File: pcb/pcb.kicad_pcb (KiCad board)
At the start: 2 copper layers, 75 x 75 mm, 4 parts, among them U1 1117-3.3

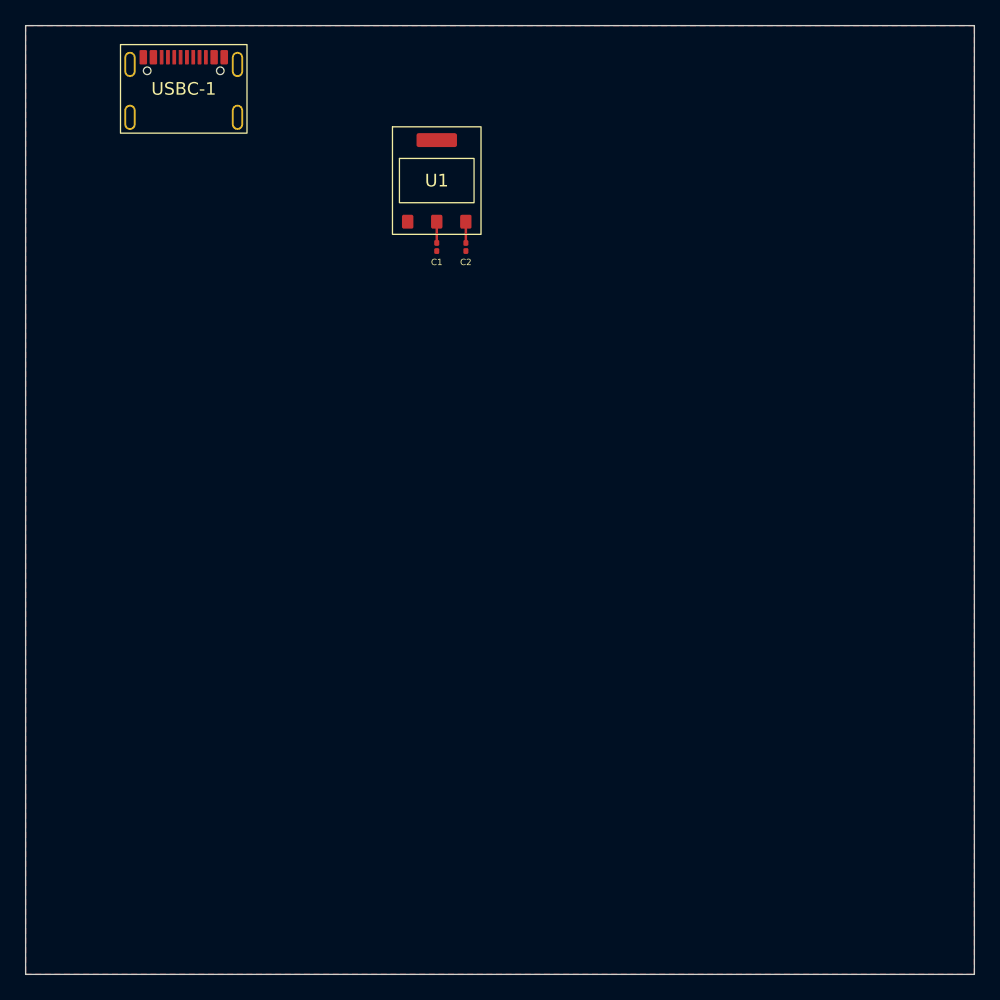
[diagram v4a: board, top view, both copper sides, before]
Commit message: add vias and ground
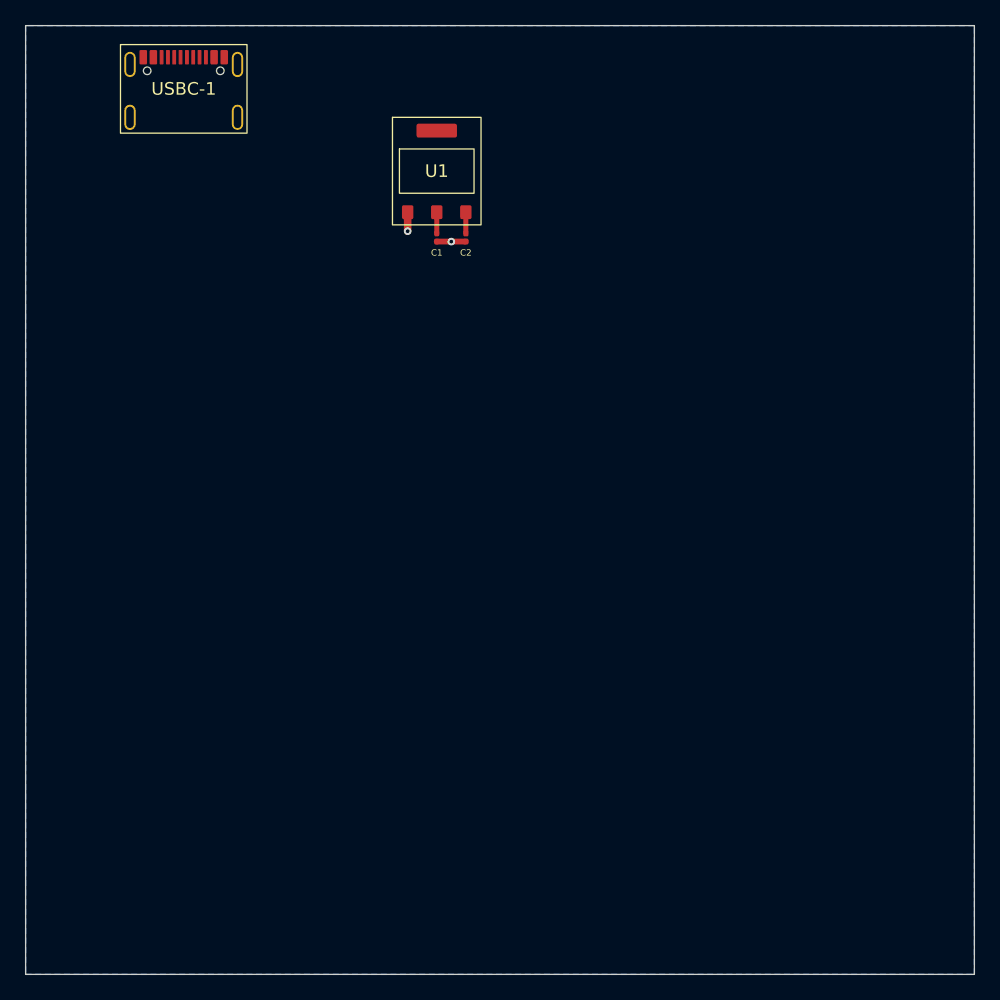
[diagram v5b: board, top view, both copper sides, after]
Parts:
- moved C1 0.75 mm to (32.5, 16.8)
- moved C2 0.75 mm to (34.8, 16.8)
- moved U1 0.75 mm to (32.5, 14.8)
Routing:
- net GND: track 0.00 -> 3.80 mm, vias 0 -> 2
- added copper zone on B.Cu, net GND
- removed copper zone on F.Cu, net GND
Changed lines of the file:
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@@
 	(footprint "Capacitor_SMD:C_0201_0603Metric"
 		(layer "F.Cu")
-		(at 32.5 17.5 90)
+		(at 32.5 16.75 90)
 		(descr "Capacitor SMD 0201 (0603 Metric), square (rectangular) end terminal, IPC-7351 nominal, (Body size source: https://www.vishay.com/docs/20052/crcw0201e3.pdf)")
 		(tags "capacitor")
@@
 	(footprint "Andrews_Library:LCSC_SMD_1117-3.3v_C5125088"
 		(layer "F.Cu")
-		(at 32.5 15.5)
+		(at 32.5 14.75)
 		(property "Reference" "U1"
 			(at 0 -3.25 0)
@@
 			(polygon
 				(pts
-					(xy 29 8) (xy 36 8) (xy 36 16.5) (xy 29 16.5)
+					(xy 29 7.25) (xy 36 7.25) (xy 36 15.75) (xy 29 15.75)
 				)
 			)
@@
 	(footprint "Capacitor_SMD:C_0201_0603Metric"
 		(layer "F.Cu")
-		(at 34.8 17.5 -90)
+		(at 34.8 16.75 -90)
 		(descr "Capacitor SMD 0201 (0603 Metric), square (rectangular) end terminal, IPC-7351 nominal, (Body size source: https://www.vishay.com/docs/20052/crcw0201e3.pdf)")
 		(tags "capacitor")
@@
 	)
 	(segment
-		(start 32.5 15.5)
-		(end 32.5 17.18)
+		(start 33.655 17.07)
+		(end 33.65 17.075)
 		(width 0.2)
 		(layer "F.Cu")
+		(net "GND")
+	)
+	(segment
+		(start 33.645 17.07)
+		(end 33.65 17.075)
+		(width 0.2)
+		(layer "F.Cu")
+		(net "GND")
+	)
+	(segment
+		(start 32.5 17.07)
+		(end 33.645 17.07)
+		(width 0.46)
+		(layer "F.Cu")
+		(net "GND")
+	)
+	(segment
+		(start 30.2 14.75)
+		(end 30.2 16.25)
+		(width 0.6)
+		(layer "F.Cu")
+		(net "GND")
+	)
+	(segment
+		(start 34.8 17.07)
+		(end 33.655 17.07)
+		(width 0.46)
+		(layer "F.Cu")
+		(net "GND")
+	)
+	(via
+		(at 30.2 16.25)
+		(size 0.6)
+		(drill 0.3)
+		(layers "F.Cu" "B.Cu")
+		(free yes)
+		(net "GND")
+	)
+	(via
+		(at 33.65 17.075)
+		(size 0.6)
+		(drill 0.3)
+		(layers "F.Cu" "B.Cu")
+		(free yes)
+		(net "GND")
+	)
+	(segment
+		(start 32.5 14.75)
+		(end 32.5 16.43)
+		(width 0.4)
+		(layer "F.Cu")
 		(net "VBUS")
 	)
 	(segment
-		(start 34.8 15.5)
-		(end 34.8 17.18)
-		(width 0.2)
+		(start 34.8 14.75)
+		(end 34.8 16.43)
+		(width 0.4)
 		(layer "F.Cu")
 		(net "Net-(U1-VIN)")
@@
 	(zone
 		(net "GND")
-		(layer "F.Cu")
+		(layer "B.Cu")
 		(hatch edge 0.5)
 		(connect_pads
@@
 		)
 	)
-	(group ""
-		(members "4c363494-5d20-44a3-9b12-37bc64127a15" "7ff470fd-2abd-486a-b746-3b467e71a7f8"
-			"a43b688b-cef3-4c08-969a-ef6623efc0b7" "c16a55e6-c9ba-4bf5-9418-845e8fc3c2c0"
-			"e2951551-5bd3-452b-943a-e5c31ddf3bfe"
-		)
-	)

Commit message: usbc schematic done?
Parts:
- moved C1 18.0 mm to (15.5, 10.7)
- moved U1 18.0 mm to (15.5, 8.72)
- moved C2 18.0 mm to (17.8, 10.7)
- moved USBC-1 6.52 mm to (6.00, 4.50)
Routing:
- net VBUS: track 1.68 -> 8.13 mm
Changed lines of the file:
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@@
 	(footprint "Capacitor_SMD:C_0201_0603Metric"
 		(layer "F.Cu")
-		(at 32.5 16.75 90)
+		(at 15.5 10.725 90)
 		(descr "Capacitor SMD 0201 (0603 Metric), square (rectangular) end terminal, IPC-7351 nominal, (Body size source: https://www.vishay.com/docs/20052/crcw0201e3.pdf)")
 		(tags "capacitor")
@@
 	(footprint "Andrews_Library:LCSC_SMD_USBC_C2760486"
 		(layer "F.Cu")
-		(at 12.5 5)
+		(at 6 4.5)
 		(property "Reference" "USBC-1"
 			(at 0 0 0)
@@
 		)
 		(property "Value" "TYPE-C-31-M-31"
-			(at 0 6.7 0)
-			(unlocked yes)
-			(layer "F.Fab")
+			(at 0 0 0)
+			(unlocked yes)
+			(layer "F.Fab")
+			(hide yes)
 			(effects
 				(font
@@
 		)
 		(fp_text user "${REFERENCE}"
-			(at 0 4.8 0)
+			(at 0 0 0)
 			(unlocked yes)
 			(layer "F.Fab")
@@
 	(footprint "Andrews_Library:LCSC_SMD_1117-3.3v_C5125088"
 		(layer "F.Cu")
-		(at 32.5 14.75)
+		(at 15.5 8.725)
 		(property "Reference" "U1"
 			(at 0 -3.25 0)
@@
 		)
 		(property "Value" "1117-3.3"
-			(at 0 -8.7 0)
-			(unlocked yes)
-			(layer "F.Fab")
+			(at 0 -3.25 0)
+			(unlocked yes)
+			(layer "F.Fab")
+			(hide yes)
 			(effects
 				(font
@@
 		)
 		(fp_text user "${REFERENCE}"
-			(at 0 -10.5 0)
+			(at 0 -3.25 0)
 			(unlocked yes)
 			(layer "F.Fab")
@@
 			(polygon
 				(pts
-					(xy 29 7.25) (xy 36 7.25) (xy 36 15.75) (xy 29 15.75)
+					(xy 12 1.225) (xy 19 1.225) (xy 19 9.725) (xy 12 9.725)
 				)
 			)
@@
 	(footprint "Capacitor_SMD:C_0201_0603Metric"
 		(layer "F.Cu")
-		(at 34.8 16.75 -90)
+		(at 17.8 10.725 -90)
 		(descr "Capacitor SMD 0201 (0603 Metric), square (rectangular) end terminal, IPC-7351 nominal, (Body size source: https://www.vishay.com/docs/20052/crcw0201e3.pdf)")
 		(tags "capacitor")
@@
 	)
 	(segment
-		(start 33.655 17.07)
-		(end 33.65 17.075)
+		(start 16.655 11.045)
+		(end 16.65 11.05)
 		(width 0.2)
 		(layer "F.Cu")
@@
 	)
 	(segment
-		(start 33.645 17.07)
-		(end 33.65 17.075)
+		(start 16.645 11.045)
+		(end 16.65 11.05)
 		(width 0.2)
 		(layer "F.Cu")
@@
 	)
 	(segment
-		(start 32.5 17.07)
-		(end 33.645 17.07)
+		(start 15.5 11.045)
+		(end 16.645 11.045)
 		(width 0.46)
 		(layer "F.Cu")
@@
 	)
 	(segment
-		(start 30.2 14.75)
-		(end 30.2 16.25)
+		(start 13.2 8.725)
+		(end 13.2 10.225)
 		(width 0.6)
 		(layer "F.Cu")
@@
 	)
 	(segment
-		(start 34.8 17.07)
-		(end 33.655 17.07)
+		(start 17.8 11.045)
+		(end 16.655 11.045)
 		(width 0.46)
 		(layer "F.Cu")
@@
 	)
 	(via
-		(at 30.2 16.25)
+		(at 13.2 10.225)
 		(size 0.6)
 		(drill 0.3)
@@
 	)
 	(via
-		(at 33.65 17.075)
+		(at 16.65 11.05)
 		(size 0.6)
 		(drill 0.3)
@@
 	)
 	(segment
-		(start 32.5 14.75)
-		(end 32.5 16.43)
+		(start 15.5 8.725)
+		(end 15.5 10.405)
 		(width 0.4)
 		(layer "F.Cu")
@@
 	)
 	(segment
-		(start 34.8 14.75)
-		(end 34.8 16.43)
+		(start 15.5 2.275)
+		(end 15.5 8.725)
+		(width 0.9)
+		(layer "F.Cu")
+		(net "VBUS")
+	)
+	(segment
+		(start 17.8 8.725)
+		(end 17.8 10.405)
 		(width 0.4)
 		(layer "F.Cu")
@@
 		)
 	)
+	(group ""
+		(members "39f46827-d604-4451-9185-d2c690da2b4b" "41b5fd87-8459-422c-bbc8-8b2f33a92733"
+			"4c363494-5d20-44a3-9b12-37bc64127a15" "60749c63-a4b9-4ef0-87bf-f6affbc0b8c7"
+			"7ff470fd-2abd-486a-b746-3b467e71a7f8" "a43b688b-cef3-4c08-969a-ef6623efc0b7"
+			"c16a55e6-c9ba-4bf5-9418-845e8fc3c2c0" "cd536c35-41a0-4b0b-8b86-075b95b23e07"
+			"cdebdc92-b3ab-437b-86b3-235f62b4ac51" "d3b7c60e-c1e7-4286-9bf0-45802d237ef3"
+			"d652f132-8de8-4c92-b180-d0c4723e5263" "dfa21c28-cfff-4090-87bf-47aef60440bb"
+			"e2951551-5bd3-452b-943a-e5c31ddf3bfe"
+		)
+	)

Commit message: usb c stuff
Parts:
- added R1: 27, Resistor_SMD:R_0201_0603Metric, F.Cu at (11.8, 9.50)
- added R2: 27, Resistor_SMD:R_0201_0603Metric, F.Cu at (12.8, 9.50)
- added R3: 5.1k, Resistor_SMD:R_0201_0603Metric, F.Cu at (13.8, 9.50)
- added R4: 5.1k, Resistor_SMD:R_0201_0603Metric, F.Cu at (10.8, 9.50)
- moved C1 22.4 mm to (32.7, 25.0)
- moved U1 22.4 mm to (32.7, 23.0)
- moved C2 22.4 mm to (35.0, 25.0)
- moved USBC-1 6.52 mm to (12.5, 5.00), turned to 180 degrees
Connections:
- USBC-1 pad A5: unconnected-(USBC-1-CC1-PadA5) -> Net-(USBC-1-CC1)
- USBC-1 pad A6: unconnected-(USBC-1-DP1-PadA6) -> Net-(USBC-1-DP1)
- USBC-1 pad A7: unconnected-(USBC-1-DN1-PadA7) -> Net-(USBC-1-DN1)
- USBC-1 pad B5: unconnected-(USBC-1-CC2-PadB5) -> Net-(USBC-1-CC2)
- USBC-1 pad B6: unconnected-(USBC-1-DP2-PadB6) -> Net-(USBC-1-DP1)
- USBC-1 pad B7: unconnected-(USBC-1-DN2-PadB7) -> Net-(USBC-1-DN1)
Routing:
- net (no net): track 0.00 -> 6.80 mm
- net Net-(USBC-1-DP1): track 0.00 -> 4.35 mm
- net Net-(USBC-1-DN1): track 0.00 -> 3.77 mm
- net GND: track 3.80 -> 5.66 mm, vias 2 -> 4
- net Net-(USBC-1-CC2): track 0.00 -> 1.68 mm
- net Net-(USBC-1-CC1): track 0.00 -> 1.68 mm

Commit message: fixxed usbc stuff
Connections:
- USBC-1 pad A1/B12: (no net) -> GND
- USBC-1 pad A4/B9: (no net) -> VBUS
- USBC-1 pad B1/A12: (no net) -> GND
- USBC-1 pad B4/A9: (no net) -> VBUS
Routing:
- net (no net): track 6.80 -> 0.00 mm
- net VBUS: track 8.13 -> 14.8 mm
- net GND: track 5.66 -> 8.24 mm
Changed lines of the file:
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@@
 			(at -1.2 0 180)
 			(layer "F.SilkS")
+			(hide yes)
 			(effects
 				(font
@@
 			(unit
 				(name "A")
-				(pins "A4" "A9" "1" "A8" "A1" "B8" "A12" "A6" "B6" "A7" "B7" "A5" "B5")
+				(pins "A4/B9" "B4/A9" "A8" "1" "B8" "A1/B12" "B1/A12" "A6" "B6" "A7"
+					"B7" "A5" "B5"
+				)
 			)
 		)
@@
 			(layers "F.Cu" "F.Mask" "F.Paste")
 			(roundrect_rratio 0.15)
+			(net "GND")
+			(pinfunction "GND_A1/B12")
+			(pintype "power_out")
 		)
 		(pad "A4/B9" smd roundrect
@@
 			(layers "F.Cu" "F.Mask" "F.Paste")
 			(roundrect_rratio 0.15)
+			(net "VBUS")
+			(pinfunction "VBUS_A4/B9")
+			(pintype "power_in")
 		)
 		(pad "A5" smd roundrect
@@
 			(layers "F.Cu" "F.Mask" "F.Paste")
 			(roundrect_rratio 0.15)
+			(net "GND")
+			(pinfunction "GND_B1/A12")
+			(pintype "power_in")
 		)
 		(pad "B4/A9" smd roundrect
@@
 			(layers "F.Cu" "F.Mask" "F.Paste")
 			(roundrect_rratio 0.15)
+			(net "VBUS")
+			(pinfunction "VBUS_B4/A9")
+			(pintype "power_in")
 		)
 		(pad "B5" smd roundrect
@@
 			(pinfunction "SBU2_B8")
 			(pintype "bidirectional+no_connect")
+		)
+		(zone
+			(layer "F.SilkS")
+			(hatch edge 0.5)
+			(connect_pads
+				(clearance 0)
+			)
+			(min_thickness 0.25)
+			(keepout
+				(tracks allowed)
+				(vias allowed)
+				(pads allowed)
+				(copperpour allowed)
+				(footprints not_allowed)
+			)
+			(placement
+				(enabled no)
+				(sheetname "")
+			)
+			(fill
+				(thermal_gap 0.5)
+				(thermal_bridge_width 0.5)
+				(island_removal_mode 0)
+			)
+			(polygon
+				(pts
+					(xy 17.5 8.5) (xy 7.5 8.5) (xy 7.5 1.5) (xy 17.5 1.5)
+				)
+			)
 		)
 		(embedded_fonts no)
@@
 			(at 1.2 0 0)
 			(layer "F.SilkS")
+			(hide yes)
 			(effects
 				(font
@@
 	)
 	(segment
-		(start 10.1 7.5)
-		(end 10.1 6.889428)
-		(width 0.4)
-		(layer "F.Cu")
-		(net "")
-	)
-	(segment
-		(start 13.960572 5.95)
-		(end 14.9 6.889428)
-		(width 0.4)
-		(layer "F.Cu")
-		(net "")
-	)
-	(segment
-		(start 11.039428 5.95)
-		(end 13.960572 5.95)
-		(width 0.4)
-		(layer "F.Cu")
-		(net "")
-	)
-	(segment
-		(start 14.9 6.889428)
-		(end 14.9 7.5)
-		(width 0.4)
-		(layer "F.Cu")
-		(net "")
-	)
-	(segment
-		(start 10.1 6.889428)
-		(end 11.039428 5.95)
-		(width 0.4)
-		(layer "F.Cu")
-		(net "")
-	)
-	(segment
 		(start 13.75 9.82)
 		(end 13.75 10.75)
@@
 	)
 	(segment
+		(start 15.7 7.5)
+		(end 16.18 7.5)
+		(width 0.6)
+		(layer "F.Cu")
+		(net "GND")
+	)
+	(segment
 		(start 33.845 25.32)
 		(end 33.85 25.325)
 		(width 0.2)
+		(layer "F.Cu")
+		(net "GND")
+	)
+	(segment
+		(start 9.3 7.5)
+		(end 8.82 7.5)
+		(width 0.6)
+		(layer "F.Cu")
+		(net "GND")
+	)
+	(segment
+		(start 8.82 7.5)
+		(end 8.25 6.93)
+		(width 0.6)
+		(layer "F.Cu")
+		(net "GND")
+	)
+	(segment
+		(start 16.18 7.5)
+		(end 16.75 6.93)
+		(width 0.6)
 		(layer "F.Cu")
 		(net "GND")
@@
 	)
 	(segment
+		(start 13.75 9.18)
+		(end 13.75 7.5)
+		(width 0.3)
+		(layer "F.Cu")
+		(net "Net-(USBC-1-CC1)")
+	)
+	(segment
+		(start 14.019999 6.05)
+		(end 14.9 6.930001)
+		(width 0.4)
+		(layer "F.Cu")
+		(net "VBUS")
+	)
+	(segment
+		(start 14.9 6.930001)
+		(end 14.9 7.5)
+		(width 0.4)
+		(layer "F.Cu")
+		(net "VBUS")
+	)
+	(segment
 		(start 32.7 23)
 		(end 32.7 24.68)
@@
 	)
 	(segment
+		(start 10.1 6.930001)
+		(end 10.980001 6.05)
+		(width 0.4)
+		(layer "F.Cu")
+		(net "VBUS")
+	)
+	(segment
+		(start 10.980001 6.05)
+		(end 14.019999 6.05)
+		(width 0.4)
+		(layer "F.Cu")
+		(net "VBUS")
+	)
+	(segment
 		(start 32.7 16.55)
 		(end 32.7 23)
@@
 	)
 	(segment
+		(start 10.1 7.5)
+		(end 10.1 6.930001)
+		(width 0.4)
+		(layer "F.Cu")
+		(net "VBUS")
+	)
+	(segment
+		(start 12.75 7.5)
+		(end 12.75 6.75)
+		(width 0.3)
+		(layer "F.Cu")
+		(net "Net-(USBC-1-DP1)")
+	)
+	(segment
+		(start 12.5 6.5)
+		(end 12.06014 6.5)
+		(width 0.3)
+		(layer "F.Cu")
+		(net "Net-(USBC-1-DP1)")
+	)
+	(segment
+		(start 11.75 6.81014)
+		(end 11.75 7.5)
+		(width 0.3)
+		(layer "F.Cu")
+		(net "Net-(USBC-1-DP1)")
+	)
+	(segment
+		(start 12.06014 6.5)
+		(end 11.75 6.81014)
+		(width 0.3)
+		(layer "F.Cu")
+		(net "Net-(USBC-1-DP1)")
+	)
+	(segment
+		(start 11.75 7.5)
+		(end 11.75 9.18)
+		(width 0.3)
+		(layer "F.Cu")
+		(net "Net-(USBC-1-DP1)")
+	)
+	(segment
+		(start 12.75 6.75)
+		(end 12.5 6.5)
+		(width 0.3)
+		(layer "F.Cu")
+		(net "Net-(USBC-1-DP1)")
+	)
+	(segment
+		(start 13.25 8.68)
+		(end 13.25 7.5)
+		(width 0.3)
+		(layer "F.Cu")
+		(net "Net-(USBC-1-DN1)")
+	)
+	(segment
+		(start 12.75 9.18)
+		(end 12.25 8.68)
+		(width 0.3)
+		(layer "F.Cu")
+		(net "Net-(USBC-1-DN1)")
+	)
+	(segment
+		(start 12.25 8.68)
+		(end 12.25 7.5)
+		(width 0.3)
+		(layer "F.Cu")
+		(net "Net-(USBC-1-DN1)")
+	)
+	(segment
+		(start 12.75 9.18)
+		(end 13.25 8.68)
+		(width 0.3)
+		(layer "F.Cu")
+		(net "Net-(USBC-1-DN1)")
+	)
+	(segment
 		(start 35 23)
 		(end 35 24.68)
@@
 		(layer "F.Cu")
 		(net "Net-(U1-VIN)")
-	)
-	(segment
-		(start 12.75 7.5)
-		(end 12.75 6.75)
-		(width 0.3)
-		(layer "F.Cu")
-		(net "Net-(USBC-1-DP1)")
-	)
-	(segment
-		(start 12.5 6.5)
-		(end 12.06014 6.5)
-		(width 0.3)
-		(layer "F.Cu")
-		(net "Net-(USBC-1-DP1)")
-	)
-	(segment
-		(start 11.75 6.81014)
-		(end 11.75 7.5)
-		(width 0.3)
-		(layer "F.Cu")
-		(net "Net-(USBC-1-DP1)")
-	)
-	(segment
-		(start 12.06014 6.5)
-		(end 11.75 6.81014)
-		(width 0.3)
-		(layer "F.Cu")
-		(net "Net-(USBC-1-DP1)")
-	)
-	(segment
-		(start 11.75 7.5)
-		(end 11.75 9.18)
-		(width 0.3)
-		(layer "F.Cu")
-		(net "Net-(USBC-1-DP1)")
-	)
-	(segment
-		(start 12.75 6.75)
-		(end 12.5 6.5)
-		(width 0.3)
-		(layer "F.Cu")
-		(net "Net-(USBC-1-DP1)")
-	)
-	(segment
-		(start 13.25 8.68)
-		(end 13.25 7.5)
-		(width 0.3)
-		(layer "F.Cu")
-		(net "Net-(USBC-1-DN1)")
-	)
-	(segment
-		(start 12.75 9.18)
-		(end 12.25 8.68)
-		(width 0.3)
-		(layer "F.Cu")
-		(net "Net-(USBC-1-DN1)")
-	)
-	(segment
-		(start 12.25 8.68)
-		(end 12.25 7.5)
-		(width 0.3)
-		(layer "F.Cu")
-		(net "Net-(USBC-1-DN1)")
-	)
-	(segment
-		(start 12.75 9.18)
-		(end 13.25 8.68)
-		(width 0.3)
-		(layer "F.Cu")
-		(net "Net-(USBC-1-DN1)")
-	)
-	(segment
-		(start 13.75 9.18)
-		(end 13.75 7.5)
-		(width 0.3)
-		(layer "F.Cu")
-		(net "Net-(USBC-1-CC1)")
 	)
 	(segment
@@
 	)
 	(group ""
-		(members "00969ec8-375b-461a-ab8d-53c311466271" "0a359fb5-a28c-437b-b3c2-884758fa63db"
-			"0c8b428b-1edc-46ec-a3d2-58d59bd35484" "0cf784ae-9619-49cc-926e-ad8379c289c3"
-			"1f80f27f-bd99-45b2-a851-89bcf631f704" "22f190ab-2413-41c7-a24e-e73d68eb9b5a"
-			"29bca4ab-ec63-4643-914a-e98f91e94fe1" "2a9f0b3c-4988-4b06-8d3b-91ca163887e9"
-			"2e3eb7c3-c9d2-411a-9390-10dacc6dc478" "3d43b053-7129-43c2-b6f8-94d0ffe57b91"
-			"42ab968e-dc35-4abf-b67d-e9f88bfc6e4c" "4b894bf6-9117-4017-9c98-93933f4364c6"
-			"50374173-e905-4b3e-b6d2-fd4c38eaf305" "6da9dd86-55fd-44dc-ad85-b6e9be5bf27e"
-			"7894b370-74d9-404b-9b6b-e3e80494a548" "80dcbed6-ae3c-4800-8257-a30dd492381d"
-			"8be4a25f-a4c5-4014-a745-92cac9a5666d" "9e8dbfe5-2635-42b1-bbe7-7b8837b5dda1"
-			"a210e89a-c73d-4a17-b1fd-acc9804ff3a6" "aeb65463-3c07-4a76-bf5e-a51c1b03362e"
-			"b25c3de0-fb7e-477a-af9d-b642d7986323" "c1df59e6-bd62-4538-8d3e-7d3726870be6"
-			"cf8427b6-465b-493e-9947-7a0465764b62" "d70bdebd-5174-401f-ab9f-6d77492b7c38"
-			"f601c40f-0a98-485b-a73e-e41fc2ebbc09" "faa3d2ee-5371-42f1-912d-1db73f624650"
+		(members "4c363494-5d20-44a3-9b12-37bc64127a15" "a4a7c4e0-1921-4a1c-82b8-160a991e9c46"
+			"c16a55e6-c9ba-4bf5-9418-845e8fc3c2c0"
 		)
 	)
 	(group ""
 		(members "39f46827-d604-4451-9185-d2c690da2b4b" "41b5fd87-8459-422c-bbc8-8b2f33a92733"
-			"4c363494-5d20-44a3-9b12-37bc64127a15" "60749c63-a4b9-4ef0-87bf-f6affbc0b8c7"
-			"7ff470fd-2abd-486a-b746-3b467e71a7f8" "a43b688b-cef3-4c08-969a-ef6623efc0b7"
-			"c16a55e6-c9ba-4bf5-9418-845e8fc3c2c0" "cd536c35-41a0-4b0b-8b86-075b95b23e07"
+			"60749c63-a4b9-4ef0-87bf-f6affbc0b8c7" "7ff470fd-2abd-486a-b746-3b467e71a7f8"
+			"a43b688b-cef3-4c08-969a-ef6623efc0b7" "cd536c35-41a0-4b0b-8b86-075b95b23e07"
 			"cdebdc92-b3ab-437b-86b3-235f62b4ac51" "d3b7c60e-c1e7-4286-9bf0-45802d237ef3"
 			"d652f132-8de8-4c92-b180-d0c4723e5263" "dfa21c28-cfff-4090-87bf-47aef60440bb"
@@
 		)
 	)
+	(group ""
+		(members "00969ec8-375b-461a-ab8d-53c311466271" "0a359fb5-a28c-437b-b3c2-884758fa63db"
+			"0c8b428b-1edc-46ec-a3d2-58d59bd35484" "0cf784ae-9619-49cc-926e-ad8379c289c3"
+			"22f190ab-2413-41c7-a24e-e73d68eb9b5a" "29bca4ab-ec63-4643-914a-e98f91e94fe1"
+			"29c53335-ca38-4edf-b1d0-7cbe707c089b" "2a9f0b3c-4988-4b06-8d3b-91ca163887e9"
+			"2e3eb7c3-c9d2-411a-9390-10dacc6dc478" "3d43b053-7129-43c2-b6f8-94d0ffe57b91"
+			"417895c3-bd0e-447a-942b-3d4d1012eba9" "42ab968e-dc35-4abf-b67d-e9f88bfc6e4c"
+			"4b894bf6-9117-4017-9c98-93933f4364c6" "5a9fd89b-1d9d-4b7a-a604-408fd6403691"
+			"6da9dd86-55fd-44dc-ad85-b6e9be5bf27e" "75d34a81-823b-4035-b028-19b2c1b16d58"
+			"7894b370-74d9-404b-9b6b-e3e80494a548" "7db35b0d-fab9-422b-8bb1-3db67172ce66"
+			"80dcbed6-ae3c-4800-8257-a30dd492381d" "88dfa8f3-c231-4c1e-8055-7ea4a8e82bd4"
+			"9e8dbfe5-2635-42b1-bbe7-7b8837b5dda1" "aeb65463-3c07-4a76-bf5e-a51c1b03362e"
+			"b25c3de0-fb7e-477a-af9d-b642d7986323" "c10a2b7c-0f63-4d39-bc5b-719cbd872340"
+			"cf8427b6-465b-493e-9947-7a0465764b62" "d1935751-456f-4883-a159-4dfe4b6ddd4c"
+			"d70bdebd-5174-401f-ab9f-6d77492b7c38" "deee6bf7-a490-4cca-a3b7-7114afd69a23"
+			"f601c40f-0a98-485b-a73e-e41fc2ebbc09" "faa3d2ee-5371-42f1-912d-1db73f624650"
+		)
+	)
